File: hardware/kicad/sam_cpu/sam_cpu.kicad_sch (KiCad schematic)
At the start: 0 parts

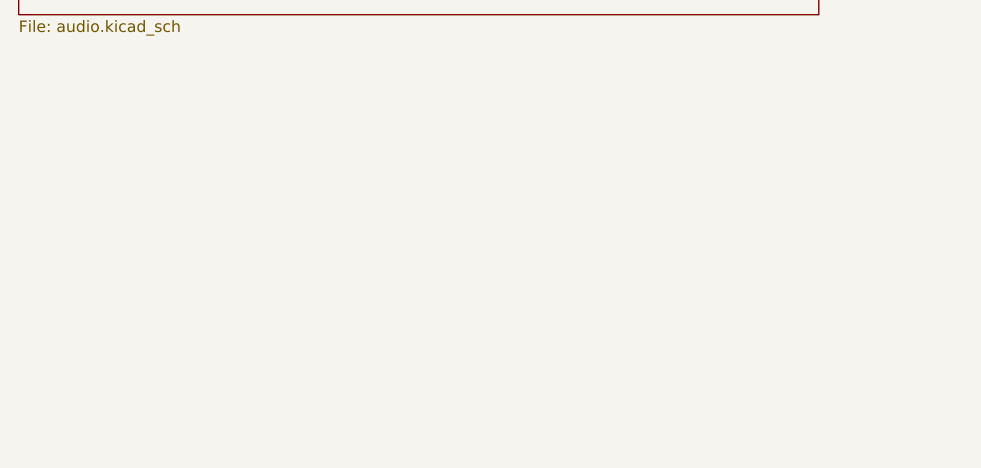
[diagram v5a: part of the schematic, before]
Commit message: Add an RS485 port (RJ45) and an I2S input header
Vincent, 2026-10-07: one RS485 port for both set-ups. With the Pi on J21
it is the Pi's UART3 (GPIO4 / 5, RTS on GPIO7 as driver enable); with a
remote Pi it is the RP2354B's UART1 (GPIO20 / 21, GPIO22 driver enable),
and the remote Pi's I2S reaches the DAC on J28. Both sides reach the
THVD1450 through 1 k, so only the configured side drives.

New page 13 (U32, R204-R212, C127, D27, JP2, J27, J28), RS485 labels on
the MCU sheet, and the 15 footprints placed without moving any part: the
RJ45 on the right edge where J5 was. README / PCB.md updated for draft 0.6
(DMD removal included). ERC clean; the new nets are not routed yet.

Co-Authored-By: Claude Opus 5.5 (1M context) <noreply@anthropic.com>
Claude-Session: https://claude.ai/code/session_01ExuDVoDDDHhVWjb8EwVzYb
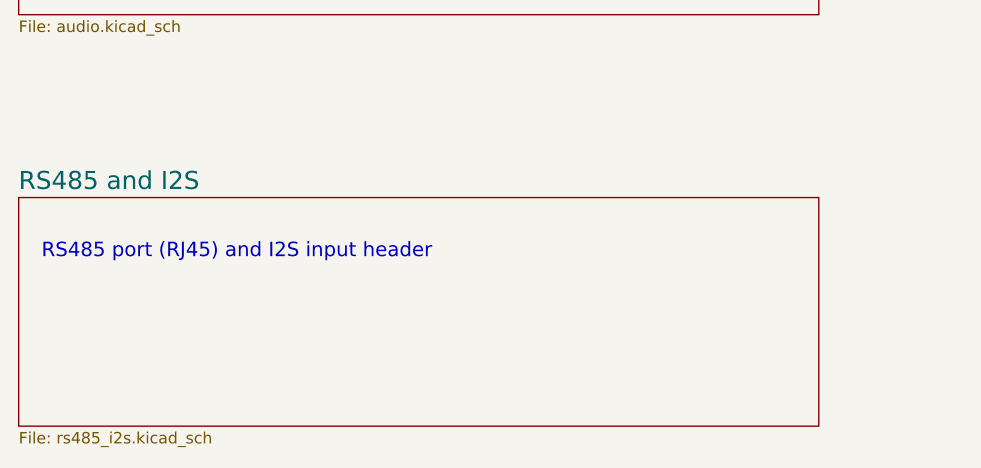
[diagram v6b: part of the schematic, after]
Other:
- added sheet RS485 and I2S (rs485_i2s.kicad_sch)
- note added: "RS485 port (RJ45) and I2S input header"
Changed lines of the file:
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@@
+	)
+	(sheet
+		(at 25.4 246.38)
+		(size 88.9 25.4)
+		(exclude_from_sim no)
+		(in_bom yes)
+		(on_board yes)
+		(dnp no)
+		(fields_autoplaced yes)
+		(stroke
+			(width 0.1524)
+			(type solid)
+		)
+		(fill
+			(color 0 0 0 0)
+		)
+		(property "Sheetname" "RS485 and I2S"
+			(at 25.4 245.6684 0)
+			(show_name no)
+			(do_not_autoplace no)
+			(effects
+				(font
+					(size 2 2)
+				)
+				(justify left bottom)
+			)
+		)
+		(property "Sheetfile" "rs485_i2s.kicad_sch"
+			(at 25.4 272.3684 0)
+			(show_name no)
+			(do_not_autoplace no)
+			(effects
+				(font
+					(size 1.27 1.27)
+				)
+				(justify left top)
+			)
+		)
+		(instances
+			(project "sam_cpu"
+				(path "/2aea4fdf-a573-57d0-a5af-7bd6ce737647"
+					(page "13")
+				)
+			)
+		)
+	)
+	(text "RS485 port (RJ45) and I2S input header"
+		(exclude_from_sim no)
+		(at 27.94 251.46 0)
+		(effects
+			(font
+				(size 1.6 1.6)
+			)
+			(justify left top)
+		)
 	)
 	(sheet

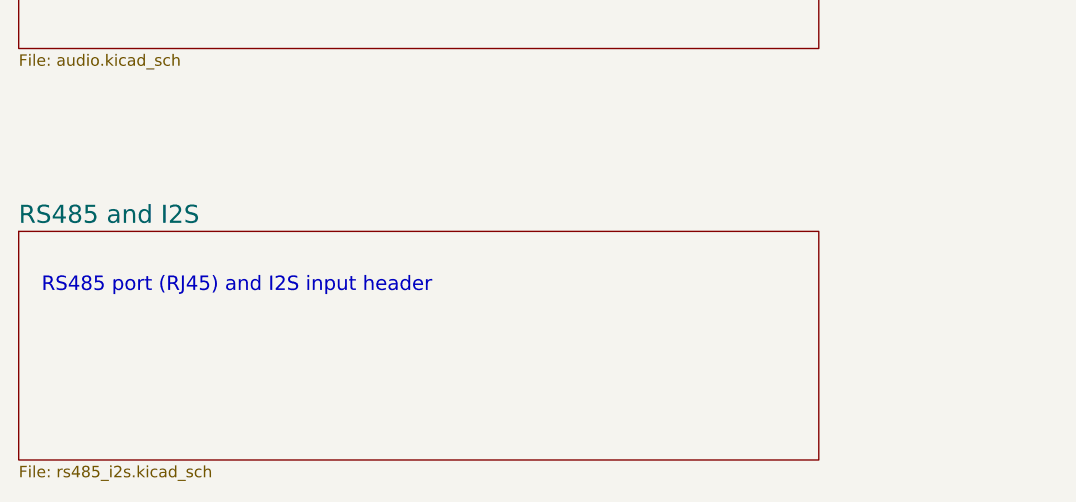
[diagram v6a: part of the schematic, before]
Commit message: Isolated RS485 (ADM2682E, two top-entry RJ45s), line-in jack, board extension back, MH3 lowered
- Page 13: ADM2682E with the cable side on GND_ISO, J27 in / J29 out (OST PJ012
  vertical), J30 switched 3.5 mm line-in between the DAC and the amplifiers.
- Audio sheet: DAC output wires split into AUD_DAC_L/R and AUD_AMP_L/R for J30.
- Board: 142 mm extension below the Pi restored, GND_ISO zone with a 2 mm gap,
  MH3 screw position moved down 7.42 mm (open notch), page-13 parts re-placed.
- Change scripts c16-c18; ERC 0, DRC schematic parity 0.

Co-Authored-By: Claude Opus 5.5 (1M context) <noreply@anthropic.com>
Claude-Session: https://claude.ai/code/session_01ExuDVoDDDHhVWjb8EwVzYb
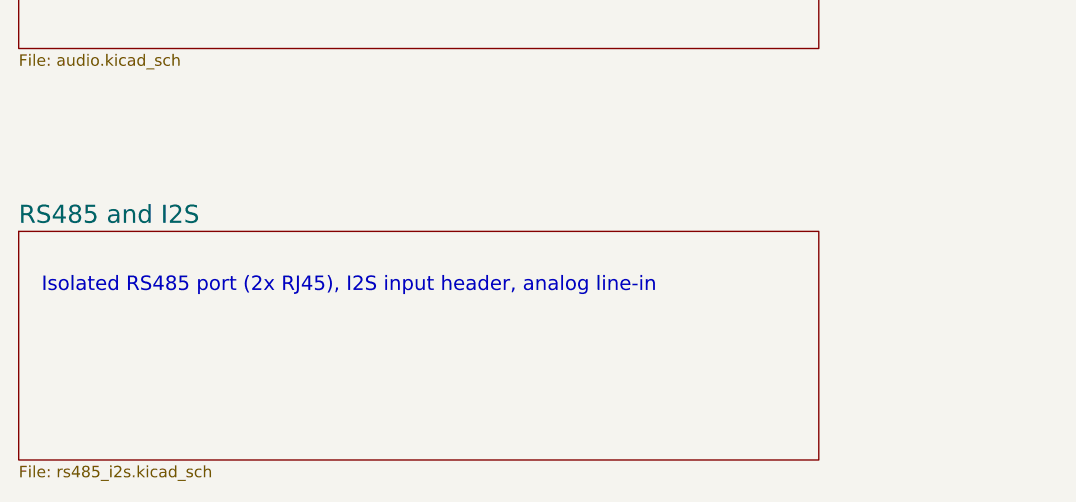
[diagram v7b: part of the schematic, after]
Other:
- note added: "Isolated RS485 port (2x RJ45), I2S input header, analog line-in"
- note removed: "RS485 port (RJ45) and I2S input header"
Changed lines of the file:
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@@
 		)
 	)
-	(text "RS485 port (RJ45) and I2S input header"
+	(text "Isolated RS485 port (2x RJ45), I2S input header, analog line-in"
 		(exclude_from_sim no)
 		(at 27.94 251.46 0)

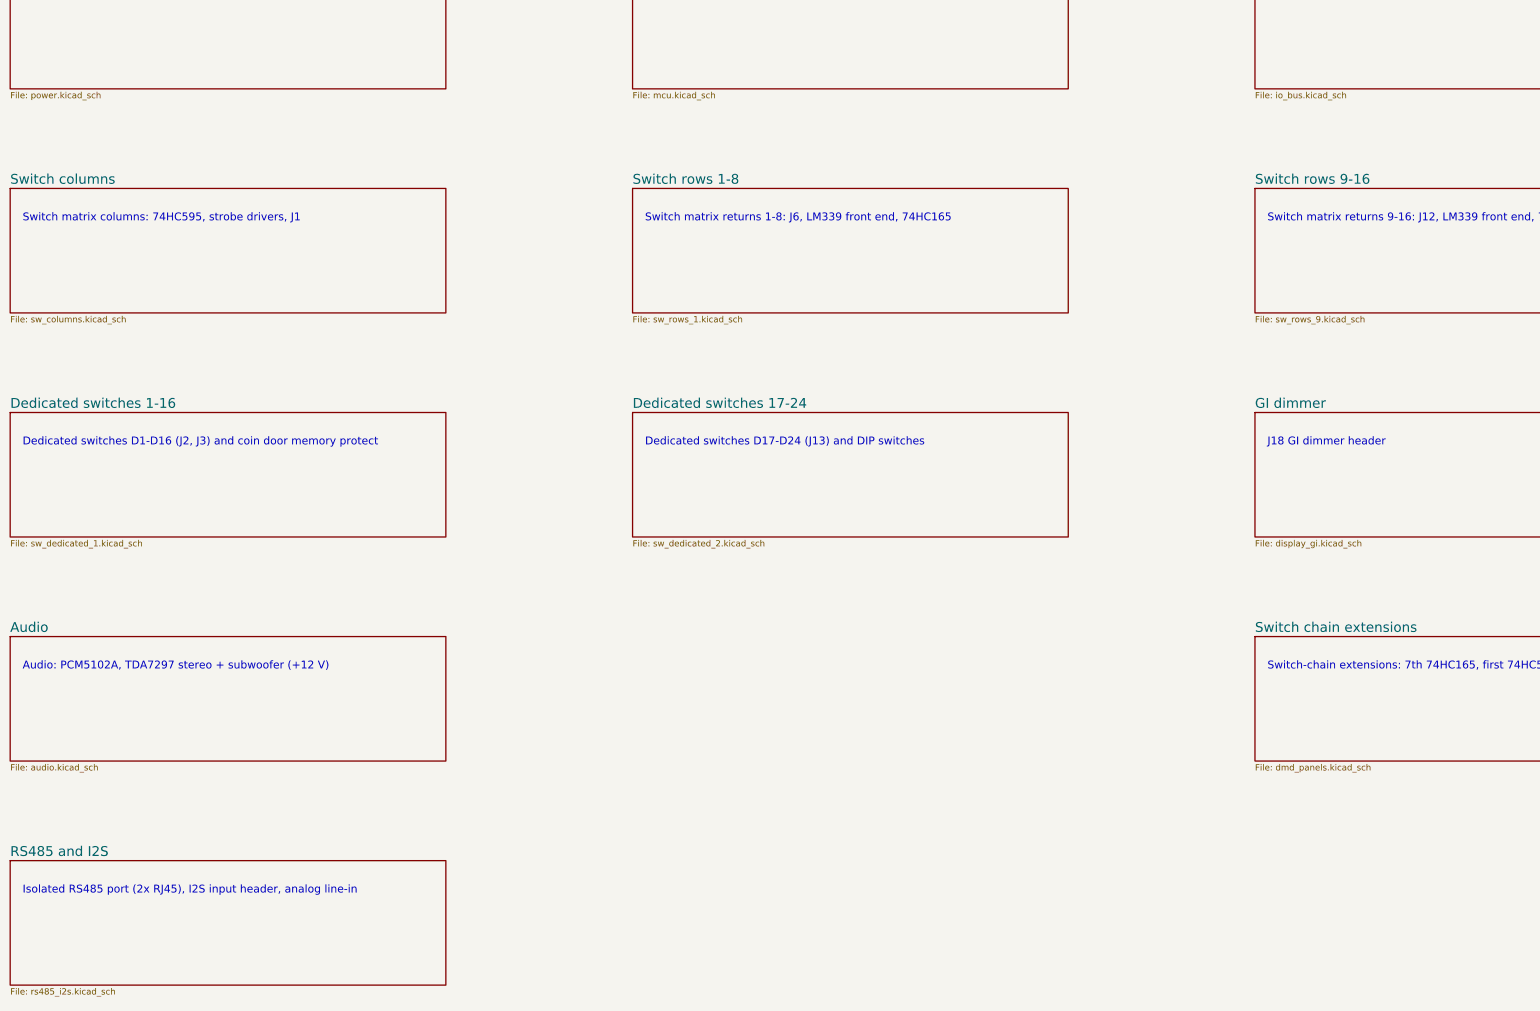
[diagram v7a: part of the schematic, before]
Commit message: DIP switch block not loaded; larger schematic text
c30: SW3, R168-R175, U14 and C93 flagged DNP (schematic and board).
c31: schematic text 1.27 -> 1.6 mm (pins 1.5 mm), intersheet refs moved out.

Co-Authored-By: Claude Opus 5.5 (1M context) <noreply@anthropic.com>
Claude-Session: https://claude.ai/code/session_01ExuDVoDDDHhVWjb8EwVzYb
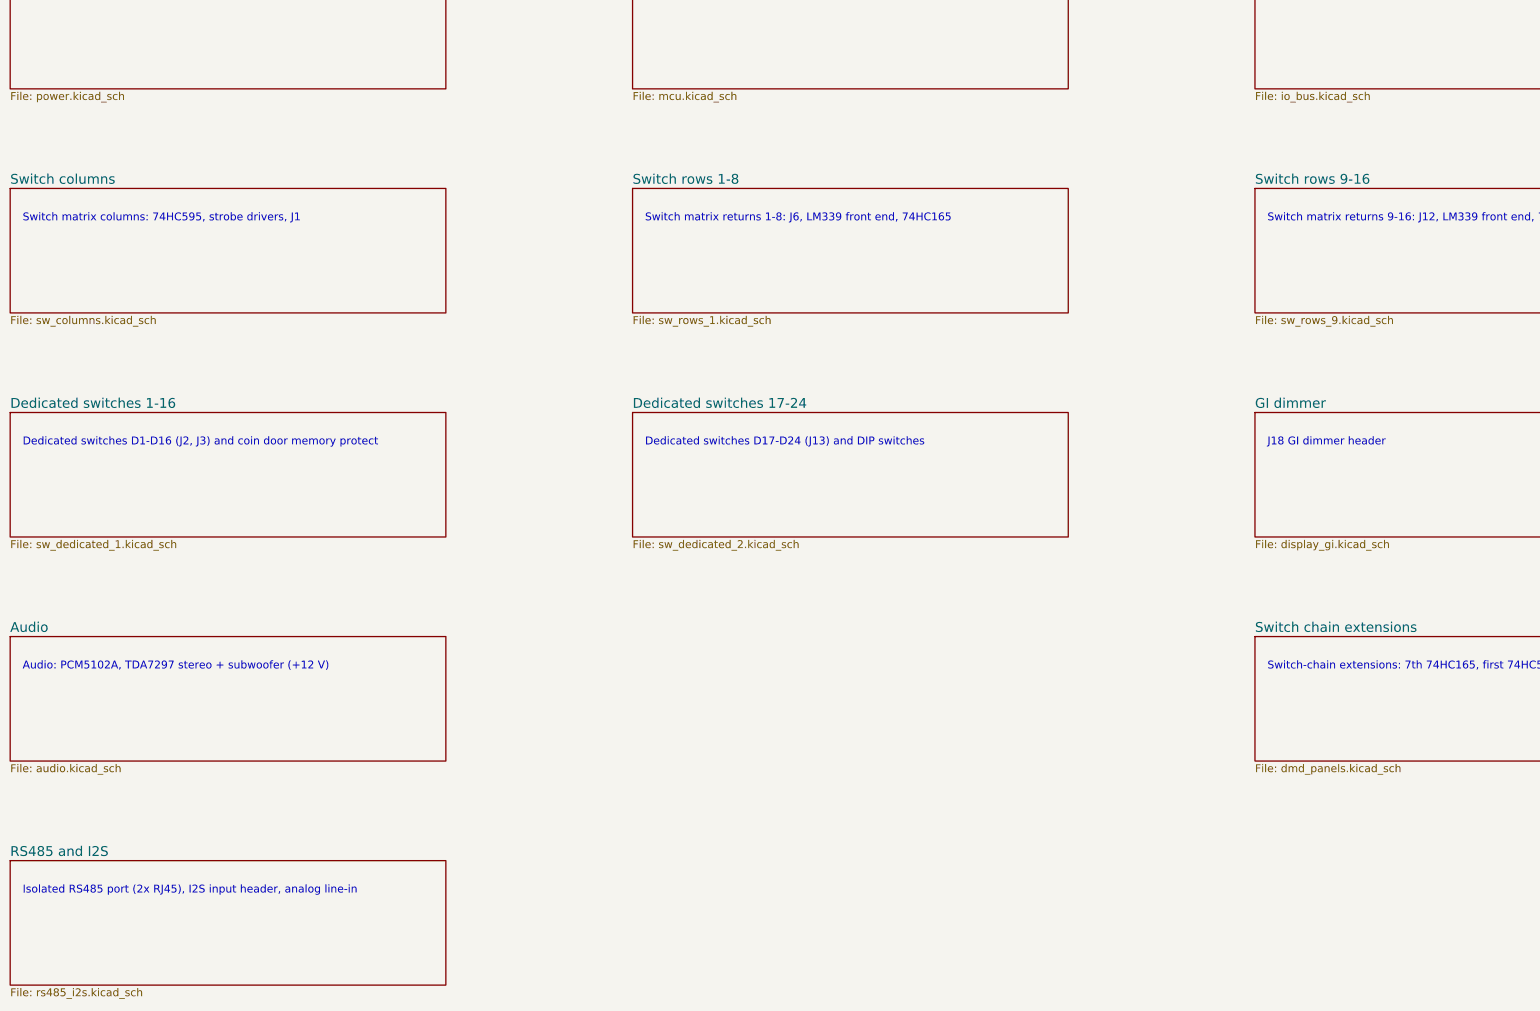
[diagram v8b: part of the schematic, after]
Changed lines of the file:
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@@
 			(effects
 				(font
-					(size 1.27 1.27)
+					(size 1.6 1.6)
 				)
 				(justify left top)
@@
 			(effects
 				(font
-					(size 1.27 1.27)
+					(size 1.6 1.6)
 				)
 				(justify left top)
@@
 			(effects
 				(font
-					(size 1.27 1.27)
+					(size 1.6 1.6)
 				)
 				(justify left top)
@@
 			(effects
 				(font
-					(size 1.27 1.27)
+					(size 1.6 1.6)
 				)
 				(justify left top)
@@
 			(effects
 				(font
-					(size 1.27 1.27)
+					(size 1.6 1.6)
 				)
 				(justify left top)
@@
 			(effects
 				(font
-					(size 1.27 1.27)
+					(size 1.6 1.6)
 				)
 				(justify left top)
@@
 			(effects
 				(font
-					(size 1.27 1.27)
+					(size 1.6 1.6)
 				)
 				(justify left top)
@@
 			(effects
 				(font
-					(size 1.27 1.27)
+					(size 1.6 1.6)
 				)
 				(justify left top)
@@
 			(effects
 				(font
-					(size 1.27 1.27)
+					(size 1.6 1.6)
 				)
 				(justify left top)
@@
 			(effects
 				(font
-					(size 1.27 1.27)
+					(size 1.6 1.6)
 				)
 				(justify left top)
@@
 			(effects
 				(font
-					(size 1.27 1.27)
+					(size 1.6 1.6)
 				)
 				(justify left top)
@@
 			(effects
 				(font
-					(size 1.27 1.27)
-				)
-				(justify left top)
+					(size 1.6 1.6)
+				)
+				(justify left top)
